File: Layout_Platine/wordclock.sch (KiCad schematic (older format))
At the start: 72 parts, among them IC1 ATMEGA8-AI, P1 DCF_CONN_4, P10 CONN_1, P101 CONN_01X02, P13 P_led, P14 CONN_2, P2 5V_CONN_2, P3 ISP, P4 UART_CONN_6, P5 Led_Zeilen_CONN_11, P6 Led_Spalten_CONN_11, P7 CONN_1, P8 CONN_1, P9 CONN_1, Q1 BC817, Q2 BC807, U1 LM317, U3 74HC04, X1 10MHz

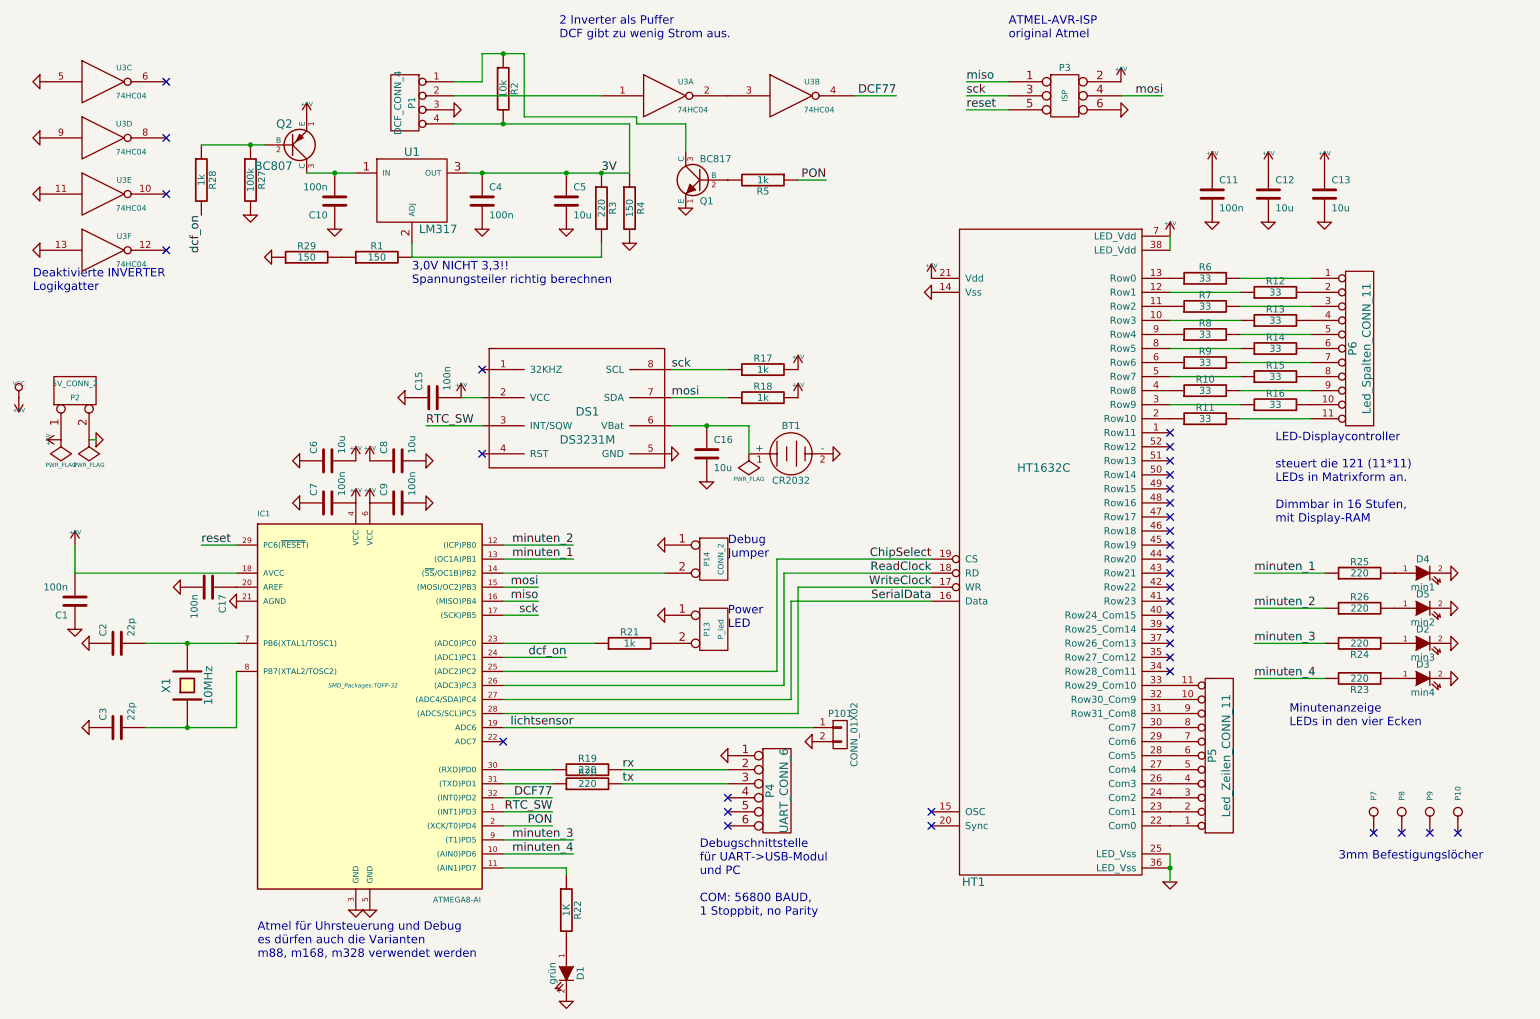
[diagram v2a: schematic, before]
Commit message: max Änderungsvorschläge wurden fast komplett umgesetzt. nur das DCF-modul ist noch nicht im Bestückungsdruck vertreten. TODO.
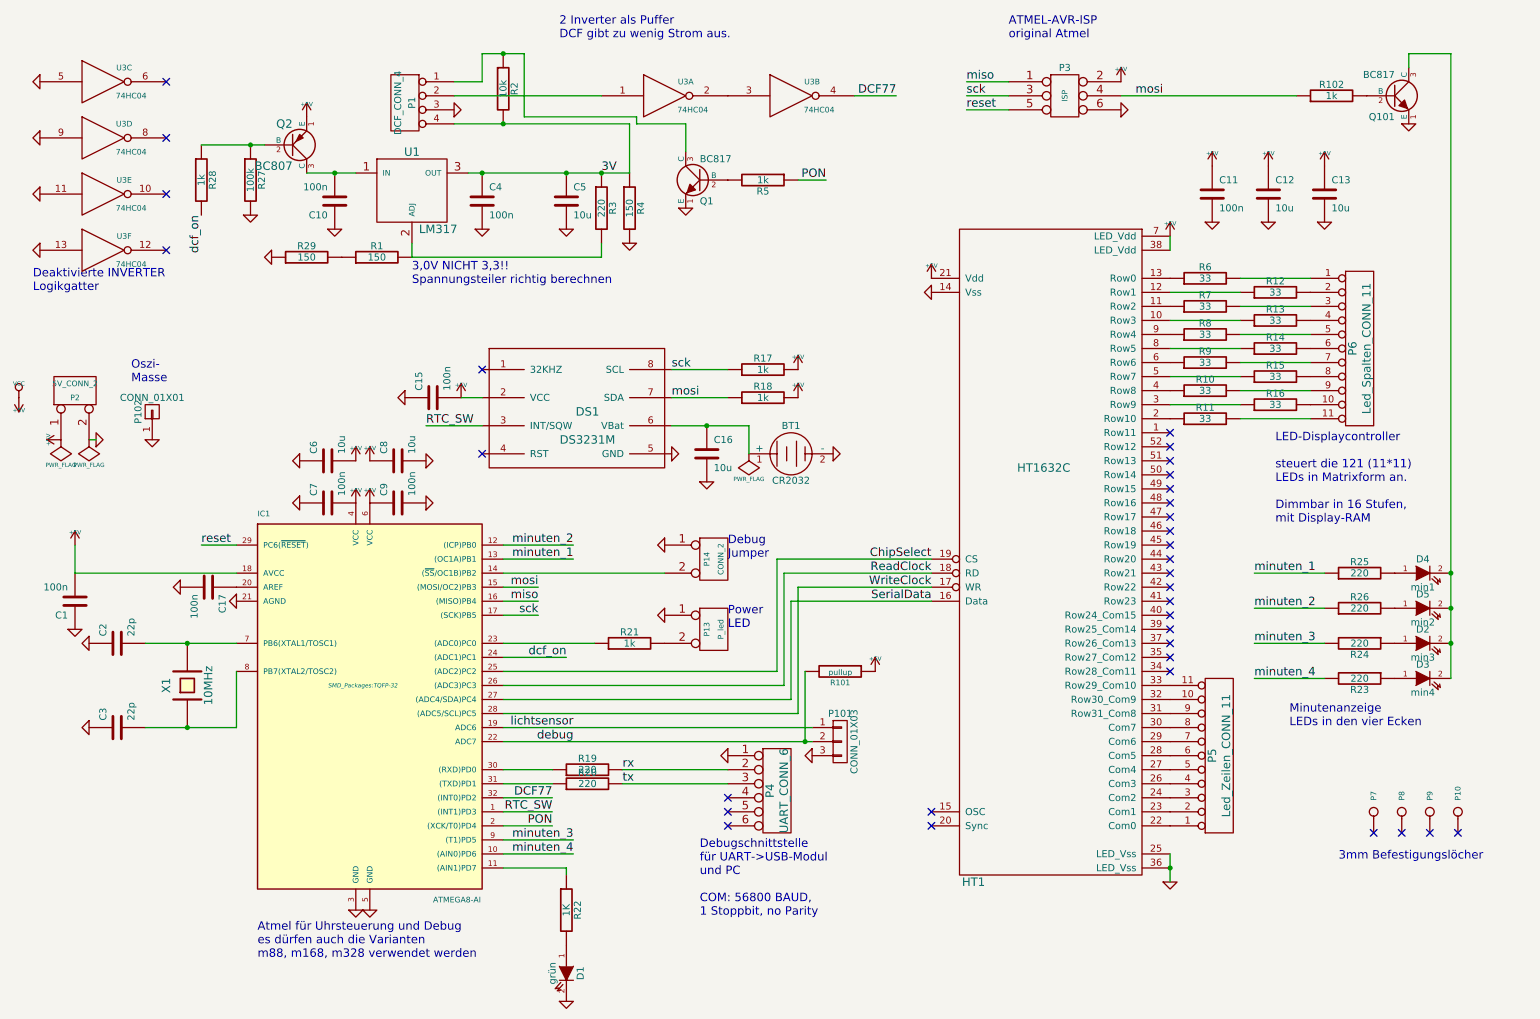
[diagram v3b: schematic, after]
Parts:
- removed P101: CONN_01X02, Pin_Headers:Pin_Header_Straight_1x02, symbol CONN_01X02
- added P101: CONN_01X03, Pin_Headers:Pin_Header_Straight_1x03, symbol CONN_01X03
- added P102: CONN_01X01, Pin_Headers:Pin_Header_Straight_1x01, symbol CONN_01X01
- added Q101: BC817, SMD_Packages:SOT-23-EBC, symbol NPN
- added R101: pullup, SMD_Packages:SMD-0805, symbol R
- added R102: 1k, SMD_Packages:SMD-0805, symbol R
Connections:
- net +5V: now also R101.1
- net GND: now also P101.3 (P3), P102.1 (P1), Q101.1 (E); no longer D2.2 (K), D3.2 (K), D4.2 (K), D5.2 (K)
- net lichtsensor: now also P101.1 (P1)
- net mosi: now also R102.1
- net debug: now reaches IC1.22 (ADC7)
- net debug: now also P101.2 (P2), R101.2
- new net: D2.2 (K), D3.2 (K), D4.2 (K), D5.2 (K), Q101.3 (C)
- new net: Q101.2 (B), R102.2
- no-connect marks 34 -> 33
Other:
- note added: "Oszi-\nMasse"

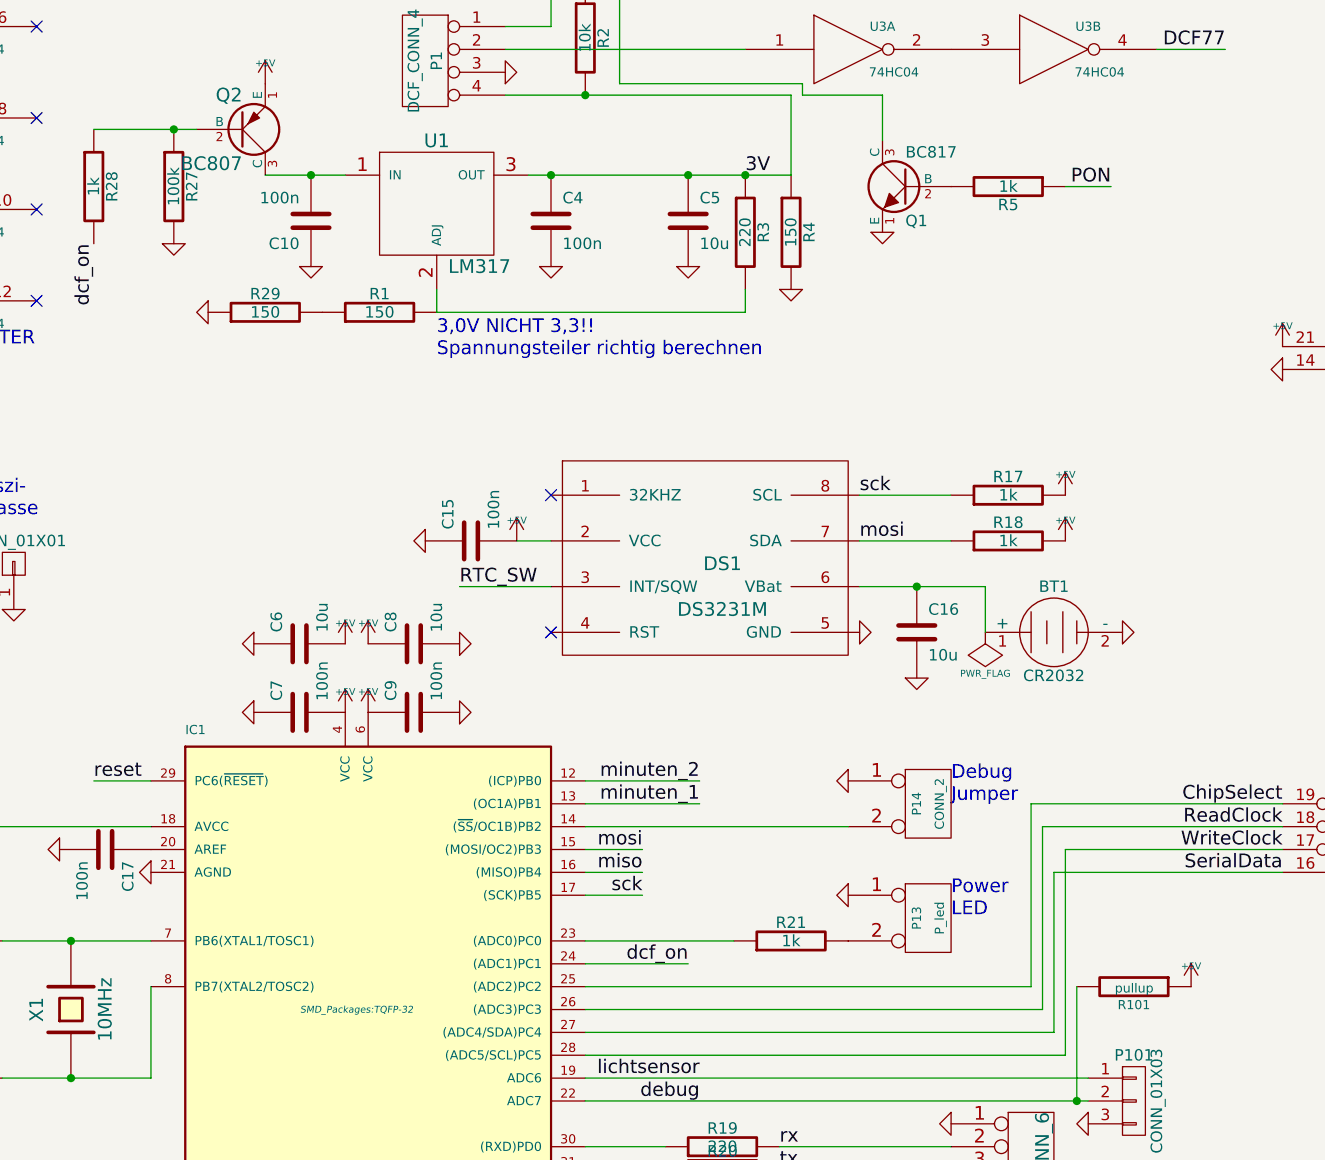
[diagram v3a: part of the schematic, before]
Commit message: gescheite BOM erstellt und hochgeladen
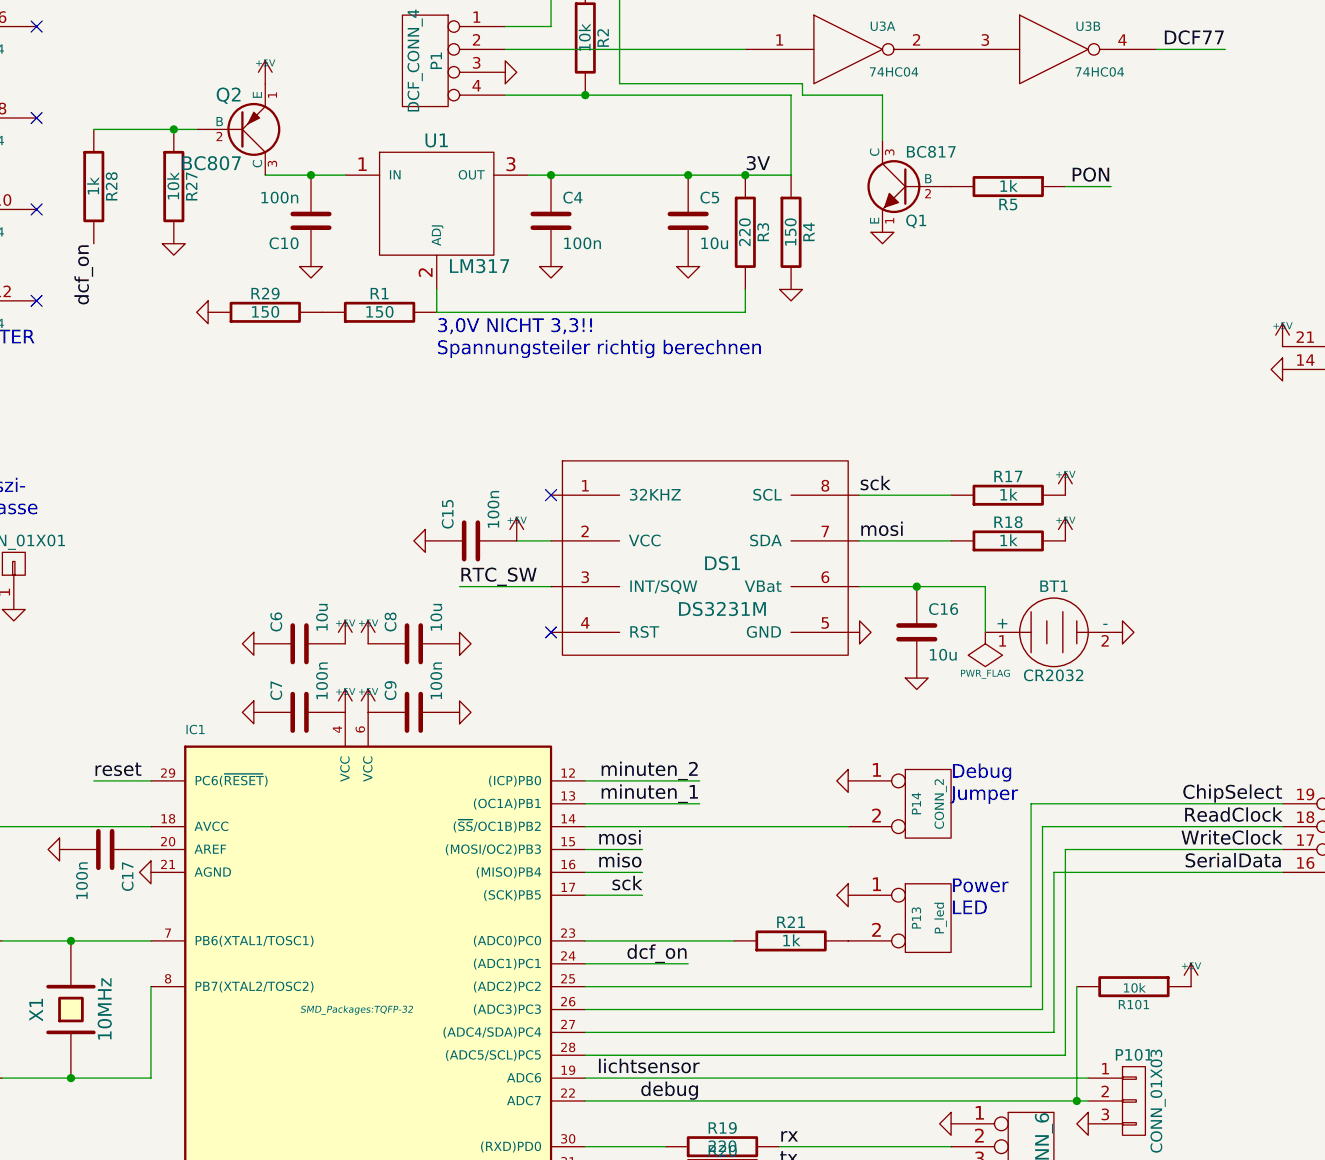
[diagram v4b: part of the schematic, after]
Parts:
- R101: value pullup -> 10k
- R27: value 100k -> 10k
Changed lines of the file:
@@
 LIBS:ds3231m
 LIBS:wordclock-cache
-EELAYER 24 0
+EELAYER 25 0
 EELAYER END
 $Descr A4 11693 8268
@@
 P 2450 1800
 F 0 "R27" V 2530 1800 50  0000 C CNN
-F 1 "100k" V 2450 1800 50  0000 C CNN
+F 1 "10k" V 2450 1800 50  0000 C CNN
 F 2 "SMD_Packages:SMD-0805" H 2450 1800 60  0001 C CNN
 F 3 "" H 2450 1800 60  0001 C CNN
@@
 P 6650 5300
 F 0 "R101" V 6730 5300 40  0000 C CNN
-F 1 "pullup" V 6657 5301 40  0000 C CNN
+F 1 "10k" V 6657 5301 40  0000 C CNN
 F 2 "SMD_Packages:SMD-0805" V 6580 5300 30  0001 C CNN
 F 3 "" H 6650 5300 30  0000 C CNN

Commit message: layout und Schaltplan für nicht-kicad-nutzer exportiert
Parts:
- C1, C10, C11, C12, C13, C15, C16, C17, C2, C3, C4, C5, C6, C7, C8, C9: symbol C -> C-RESCUE-wordclock
- D1, D2, D3, D4, D5: symbol LED -> LED-RESCUE-wordclock
- R1, R10, R101, R102, R11, R12, R13, R14, R15, R16, R17, R18, R19, R2, R20, R21, R22, R23, R24, R25, R26, R27, R28, R29, R3, R4, R5, R6, R7, R8, R9: symbol R -> R-RESCUE-wordclock
